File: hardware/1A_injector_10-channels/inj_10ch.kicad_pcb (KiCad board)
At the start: 2 copper layers, 47.6 x 56.5 mm, 56 parts, among them P1 CONN_3, P2 CONN_10X2, P3 CONN_14, Q1 OVP_DRIVER, Q10 OVP_DRIVER, Q11 OVP_DRIVER, Q12 OVP_DRIVER, Q2 OVP_DRIVER, Q3 OVP_DRIVER, Q4 OVP_DRIVER, Q5 OVP_DRIVER, Q6 OVP_DRIVER, Q7 OVP_DRIVER, Q8 OVP_DRIVER, Q9 OVP_DRIVER

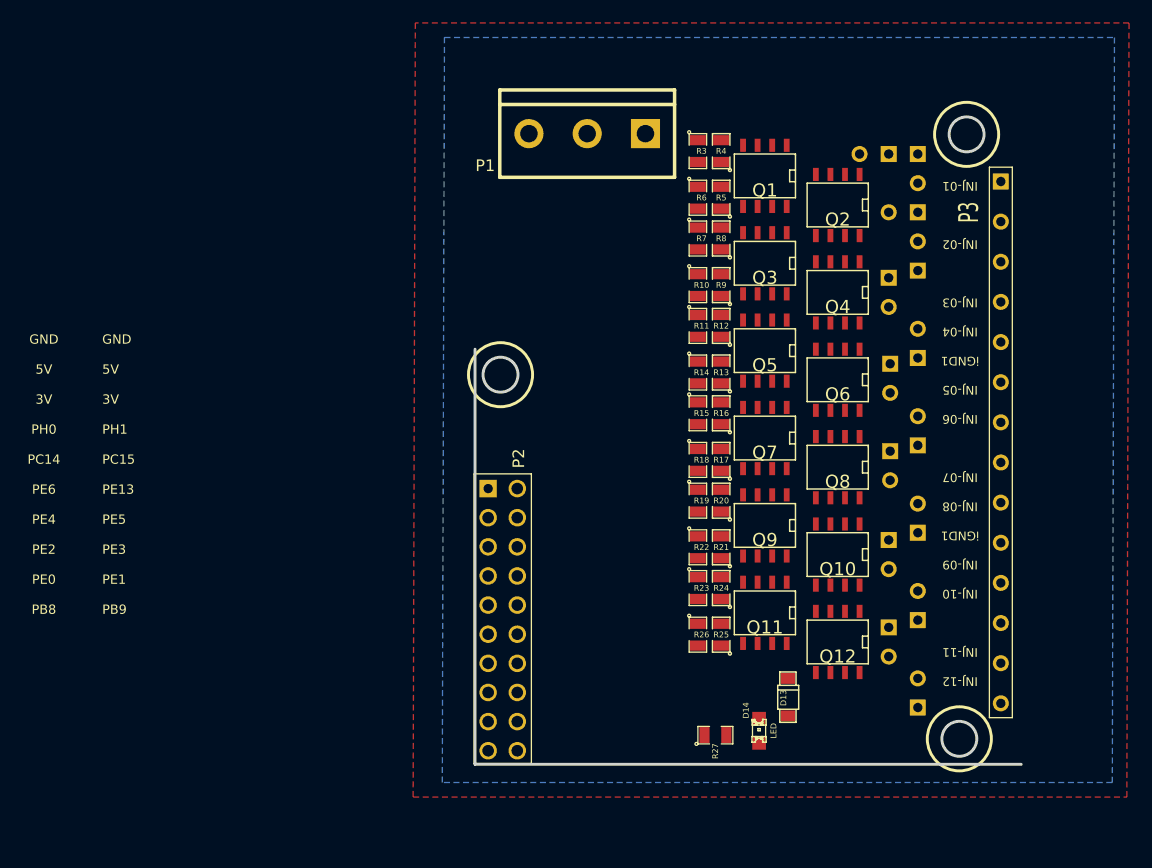
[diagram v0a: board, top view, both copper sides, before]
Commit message: 
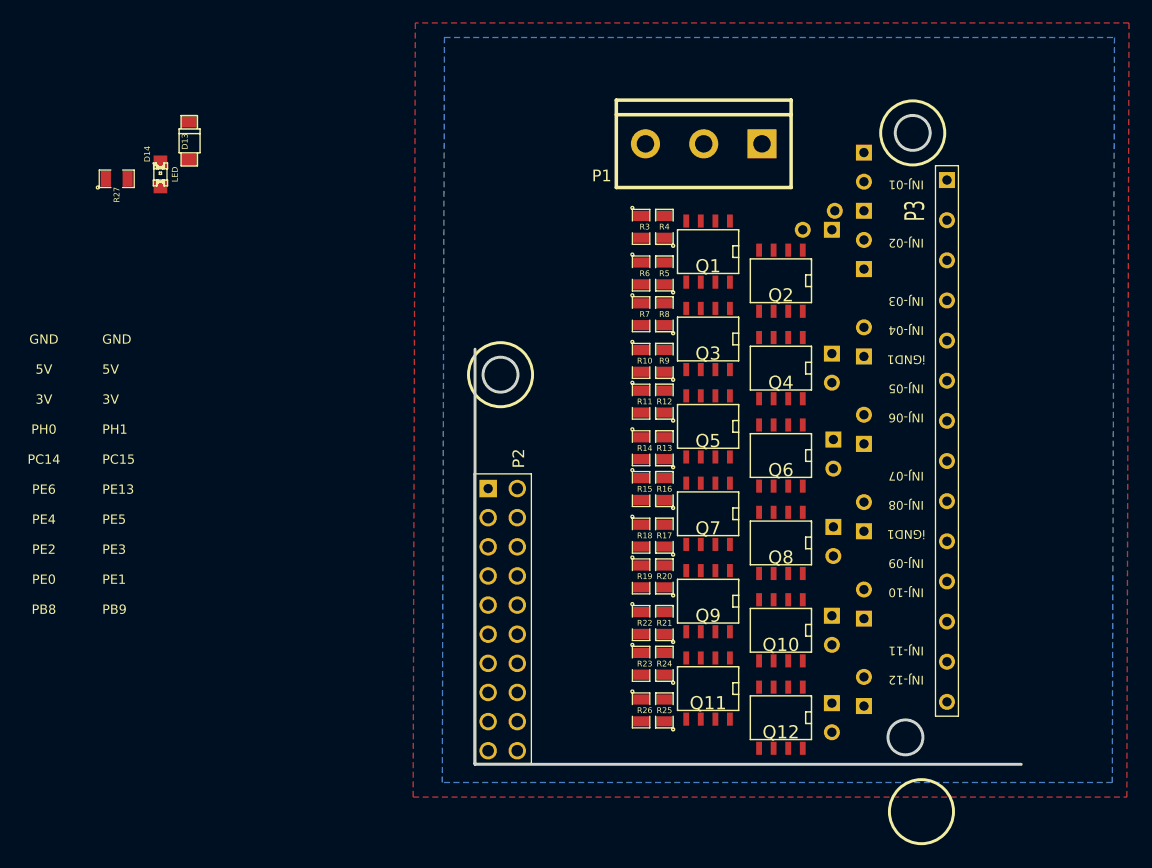
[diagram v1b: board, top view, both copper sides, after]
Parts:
- moved D13 71.3 mm to (151.8, 96.6)
- moved D14 71.3 mm to (149.2, 99.6)
- moved R27 71.3 mm to (145.4, 99.9)
- moved P1 10.2 mm to (196.6, 96.9)
- moved Q1 8.26 mm to (197.0, 106.3)
- moved Q11 8.26 mm to (197.0, 144.4)
- moved Q8 8.26 mm to (203.3, 131.7)
- moved R19 8.26 mm to (191.1, 134.6)
- moved R20 8.26 mm to (193.2, 134.6)
- moved R23 8.26 mm to (191.1, 142.2)
- moved R24 8.26 mm to (193.2, 142.2)
- moved R25 8.26 mm to (193.2, 146.3)
- moved R26 8.26 mm to (191.1, 146.3)
- moved D3 8.26 mm to (207.8, 116.5)
- moved D5 8.26 mm to (207.9, 124.0)
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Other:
- board size 47.6 x 56.5 mm -> 47.6 x 56.6 mm

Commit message: better layout
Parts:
- moved D13 33.8 mm to (184.4, 105.6)
- moved D14 33.8 mm to (181.9, 108.5)
- moved R27 33.8 mm to (178.1, 108.9)
- moved R1 4.16 mm to (207.0, 100.3), turned to 270 degrees
- moved D10 3.72 mm to (209.5, 140.6)
- moved D12 3.72 mm to (209.5, 148.2)
- moved R2 3.72 mm to (208.2, 106.3)
- moved D1 3.72 mm to (209.5, 102.5)
- moved D2 3.72 mm to (209.5, 110.1)
- moved D4 3.72 mm to (209.5, 117.7)
- moved D6 3.72 mm to (209.5, 125.3)
- moved P3 3.72 mm to (216.7, 126.4)
- moved D8 3.72 mm to (209.5, 133.0)
- moved D7 3.28 mm to (207.1, 128.4)
- moved D3 3.28 mm to (206.9, 113.3)
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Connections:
- net /3V renamed /3.3V
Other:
- board size 47.6 x 56.6 mm -> 47.6 x 55.2 mm

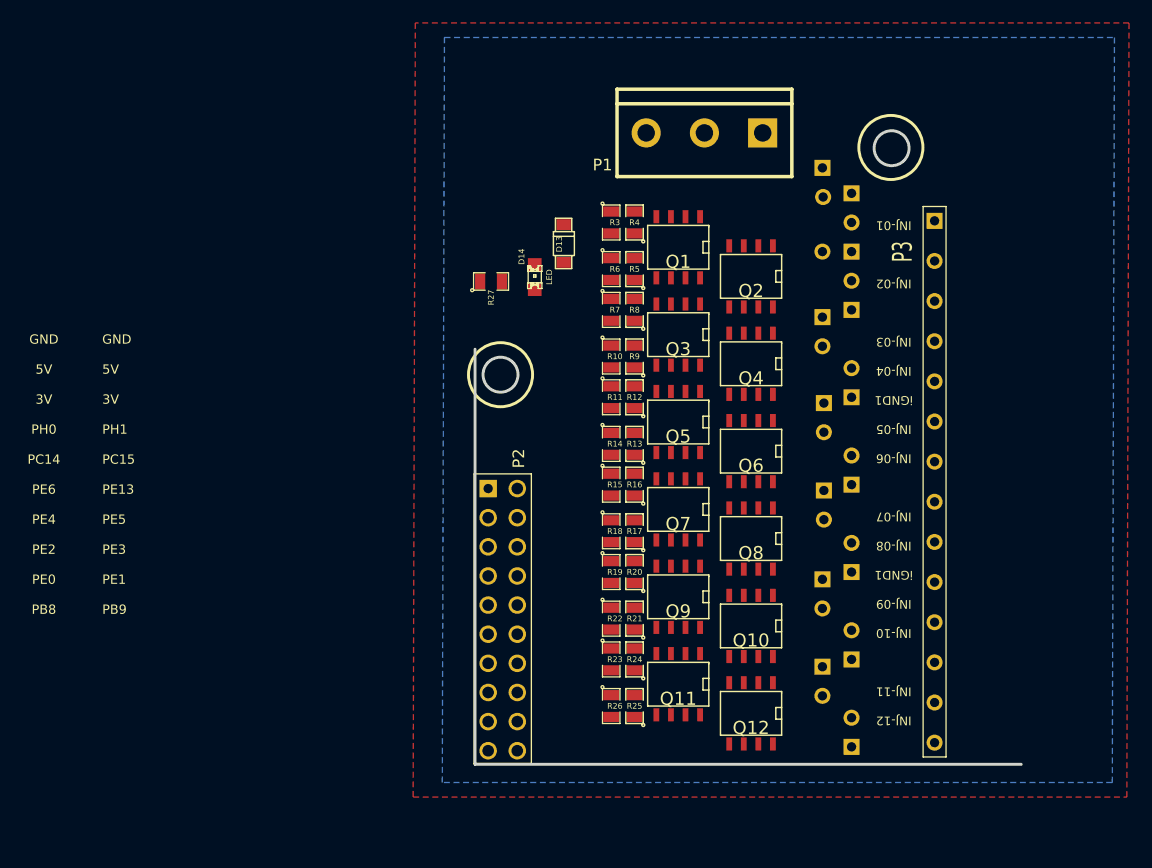
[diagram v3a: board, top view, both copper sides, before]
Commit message: 
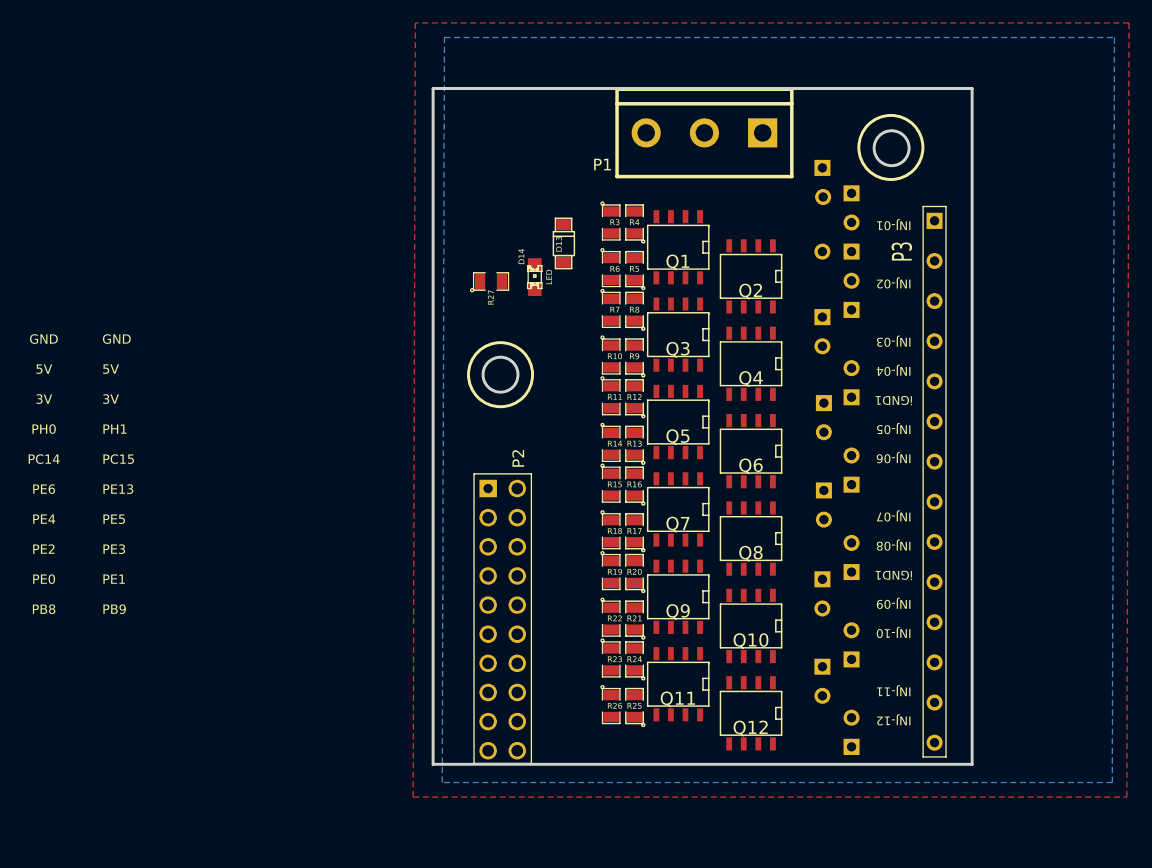
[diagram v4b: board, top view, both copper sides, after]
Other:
- board size 47.6 x 55.2 mm -> 47 x 58.9 mm
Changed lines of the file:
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@@
     (area 120.639999 86.36 233.680001 190.510001)
     (thickness 1.6002)
-    (drawings 46)
+    (drawings 48)
     (tracks 0)
     (zones 0)
@@
     )
   )
+  (gr_line (start 220 92.075) (end 220 151.003) (angle 90) (layer Edge.Cuts) (width 0.254))
+  (gr_line (start 173 92.075) (end 220 92.075) (angle 90) (layer Edge.Cuts) (width 0.254))
   (gr_text iGND1 (at 213.1695 134.493 180) (layer F.SilkS)
     (effects (font (size 0.762 0.762) (thickness 0.1143)))
@@
     (effects (font (size 0.8128 0.8128) (thickness 0.127)))
   )
-  (gr_line (start 224.282 151.003) (end 176.657 151.003) (angle 90) (layer Edge.Cuts) (width 0.254))
-  (gr_line (start 176.657 151.003) (end 176.657 114.808) (angle 90) (layer Edge.Cuts) (width 0.254))
+  (gr_line (start 220 151.003) (end 173 151.003) (angle 90) (layer Edge.Cuts) (width 0.254))
+  (gr_line (start 173 151.003) (end 173 92.075) (angle 90) (layer Edge.Cuts) (width 0.254))
   (gr_circle (center 178.8795 117.0305) (end 181.6735 117.0305) (layer F.SilkS) (width 0.254))
   (gr_text "DAECU\nrev A.02" (at 209.042 128.905 180) (layer B.SilkS)

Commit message: looks nice!
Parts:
- added P4: CONN_1, PINTST, B.Cu at (176.5, 135.9)
- added P5: CONN_1, PINTST, B.Cu at (181.6, 133.3)
- moved R27 22.8 mm to (199.4, 101.0)
- moved D14 20.2 mm to (201.3, 102.9), turned to 0 degrees
- moved D13 20.0 mm to (203.8, 101.0), turned to 0 degrees
- moved R1 0.57 mm to (207.0, 99.7), turned to 90 degrees
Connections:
- net /3.3V renamed /3V
- D13 pad 2: /INJ-12 -> /INJ-01
- P2 pad 10: (no net) -> /INJ-02_5V
- P2 pad 11: /INJ-11_5V -> /INJ-03_5V
- P2 pad 12: /INJ-05_5V -> /INJ-04_5V
- P2 pad 13: /INJ-10_5V -> /INJ-05_5V
- P2 pad 14: /INJ-04_5V -> /INJ-06_5V
- P2 pad 15: /INJ-09_5V -> /INJ-07_5V
- P2 pad 16: /INJ-03_5V -> /INJ-08_5V
- P2 pad 17: /INJ-08_5V -> /INJ-09_5V
- P2 pad 18: /INJ-02_5V -> /INJ-10_5V
- P2 pad 19: /INJ-07_5V -> /INJ-11_5V
- P2 pad 20: /INJ-01_5V -> /INJ-12_5V
- P2 pad 7: (no net) -> /PH0
- P2 pad 8: (no net) -> /PH1
- P2 pad 9: /INJ-12_5V -> /INJ-01_5V
- R14 pad 2: /INJ-07_5V -> /INJ-06_5V
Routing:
- net GND: track 0.00 -> 435.2 mm, vias 0 -> 187
- net /5V: track 0.00 -> 65.2 mm
- net /3V: track 0.00 -> 53.4 mm
- net /INJ-01_5V: track 0.00 -> 38.6 mm
- net /INJ-02_5V: track 0.00 -> 33.7 mm
- net /INJ-03_5V: track 0.00 -> 33.6 mm
- net /INJ-05_5V: track 0.00 -> 29.3 mm
- net /INJ-04_5V: track 0.00 -> 28.6 mm
- net /INJ-03: track 0.00 -> 28.0 mm
- net /INJ-07: track 0.00 -> 27.2 mm
- net /INJ-09: track 0.00 -> 27.1 mm
- net /INJ-11: track 0.00 -> 26.8 mm
- net /INJ-05: track 0.00 -> 26.8 mm
- net /INJ-07_5V: track 0.00 -> 24.8 mm
- net /INJ-06_5V: track 0.00 -> 24.2 mm
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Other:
- board text added: "DAECU rev A.01"
- board text added: "for rusefi.com"
- board text added: "http://code.google.com/p/daecu/"
- board text removed: "DAECU rev A.02"
- board text removed: "https://code.google.com/p/daecu/ for rusefi.com rev 0.1"

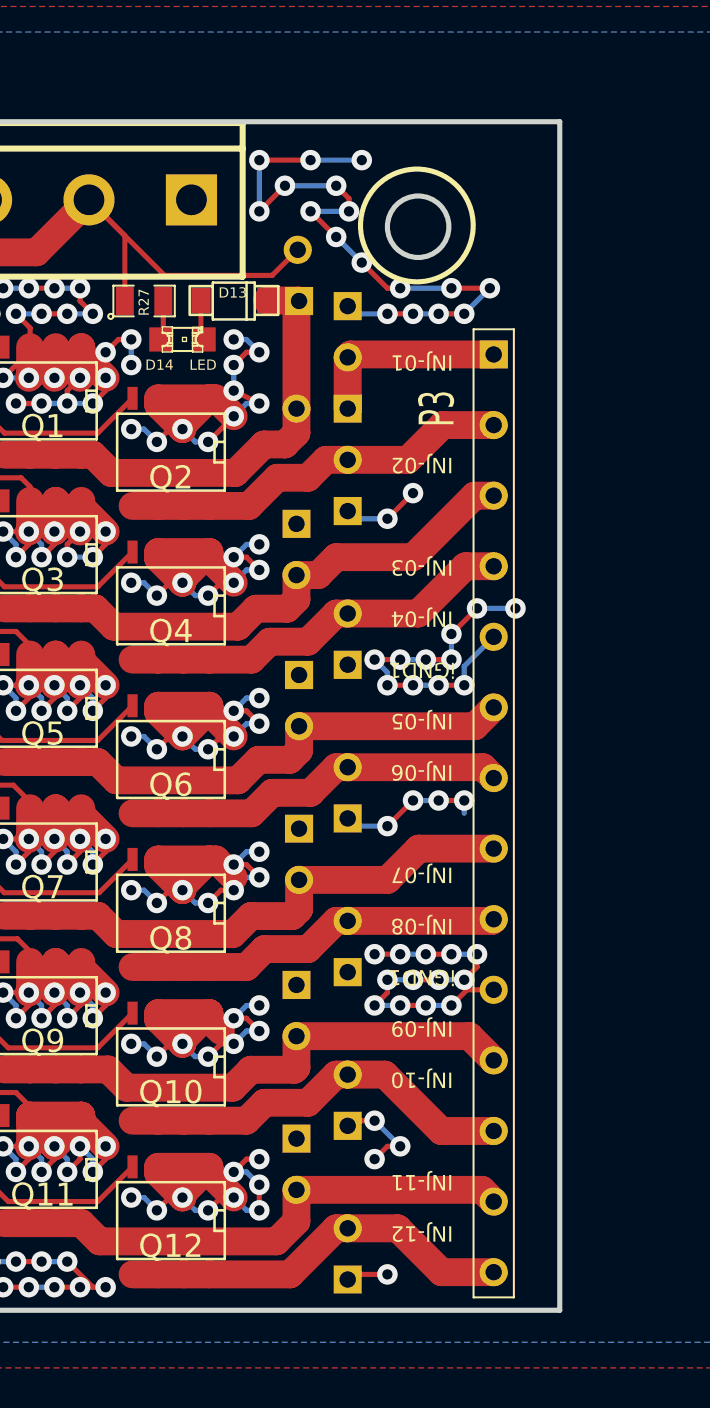
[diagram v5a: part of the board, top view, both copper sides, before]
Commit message: 
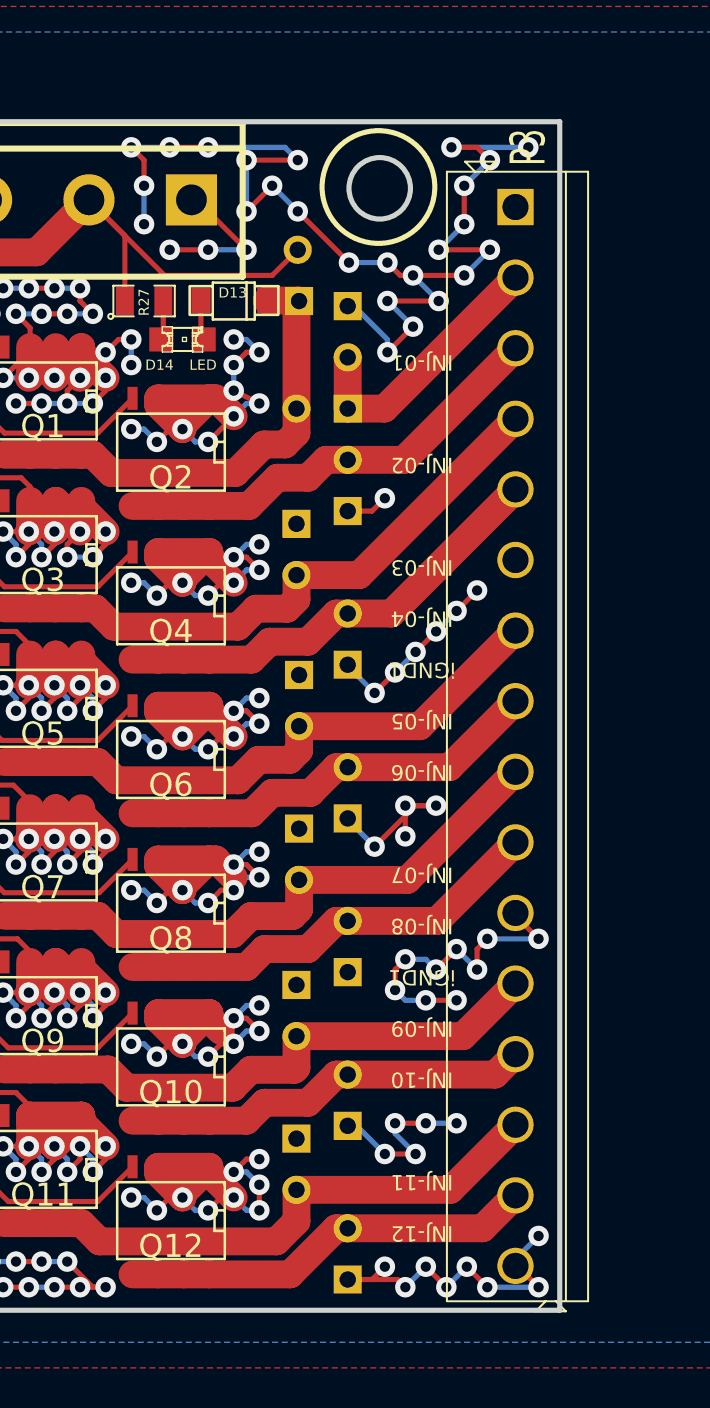
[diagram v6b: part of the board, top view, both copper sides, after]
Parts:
- P3: value CONN_14 -> CONN_16; footprint SIL-14 -> SIL-16_3.5MM
- moved P3 3.96 mm to (217.8, 122.6)
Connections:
- P3 pad 1: /INJ-01_2 -> GND
- P3 pad 10: GND -> /INJ-08
- P3 pad 11: /INJ-09 -> GND
- P3 pad 12: /INJ-10 -> /INJ-09
- P3 pad 13: /INJ-11 -> /INJ-10
- P3 pad 14: /INJ-12 -> /INJ-11
- P3 pad 2: /INJ-02 -> /INJ-01_2
- P3 pad 3: /INJ-03 -> /INJ-02
- P3 pad 4: /INJ-04 -> /INJ-03
- P3 pad 5: GND -> /INJ-04
- P3 pad 6: /INJ-05 -> GND
- P3 pad 7: /INJ-06 -> /INJ-05
- P3 pad 8: /INJ-07 -> /INJ-06
- P3 pad 9: /INJ-08 -> /INJ-07
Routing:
- net GND: track 435.2 -> 475.5 mm, vias 187 -> 197
- net /INJ-01_2: track 9.84 -> 13.5 mm
- net /INJ-07: track 27.2 -> 29.9 mm
- net /INJ-08: track 18.9 -> 21.5 mm
- net /INJ-05: track 26.8 -> 29.5 mm
- net /INJ-04: track 19.8 -> 22.5 mm
- net /INJ-03: track 28.0 -> 30.7 mm
- net /INJ-02: track 19.6 -> 22.2 mm
- net /INJ-06: track 19.1 -> 21.3 mm
- net /INJ-11: track 26.8 -> 29.0 mm
- net /INJ-09: track 27.1 -> 28.8 mm
- net /INJ-12: track 19.8 -> 20.6 mm
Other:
- outline, holes or cut-outs redrawn
